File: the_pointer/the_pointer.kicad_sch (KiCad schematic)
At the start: 19 parts, among them U1 ESP32-S2FH4, U10 TPS61033DRLR, U101 ESP32-S3FN8, U2 W25Q128JVS, X2 XRCGB40M000F1S2GR0

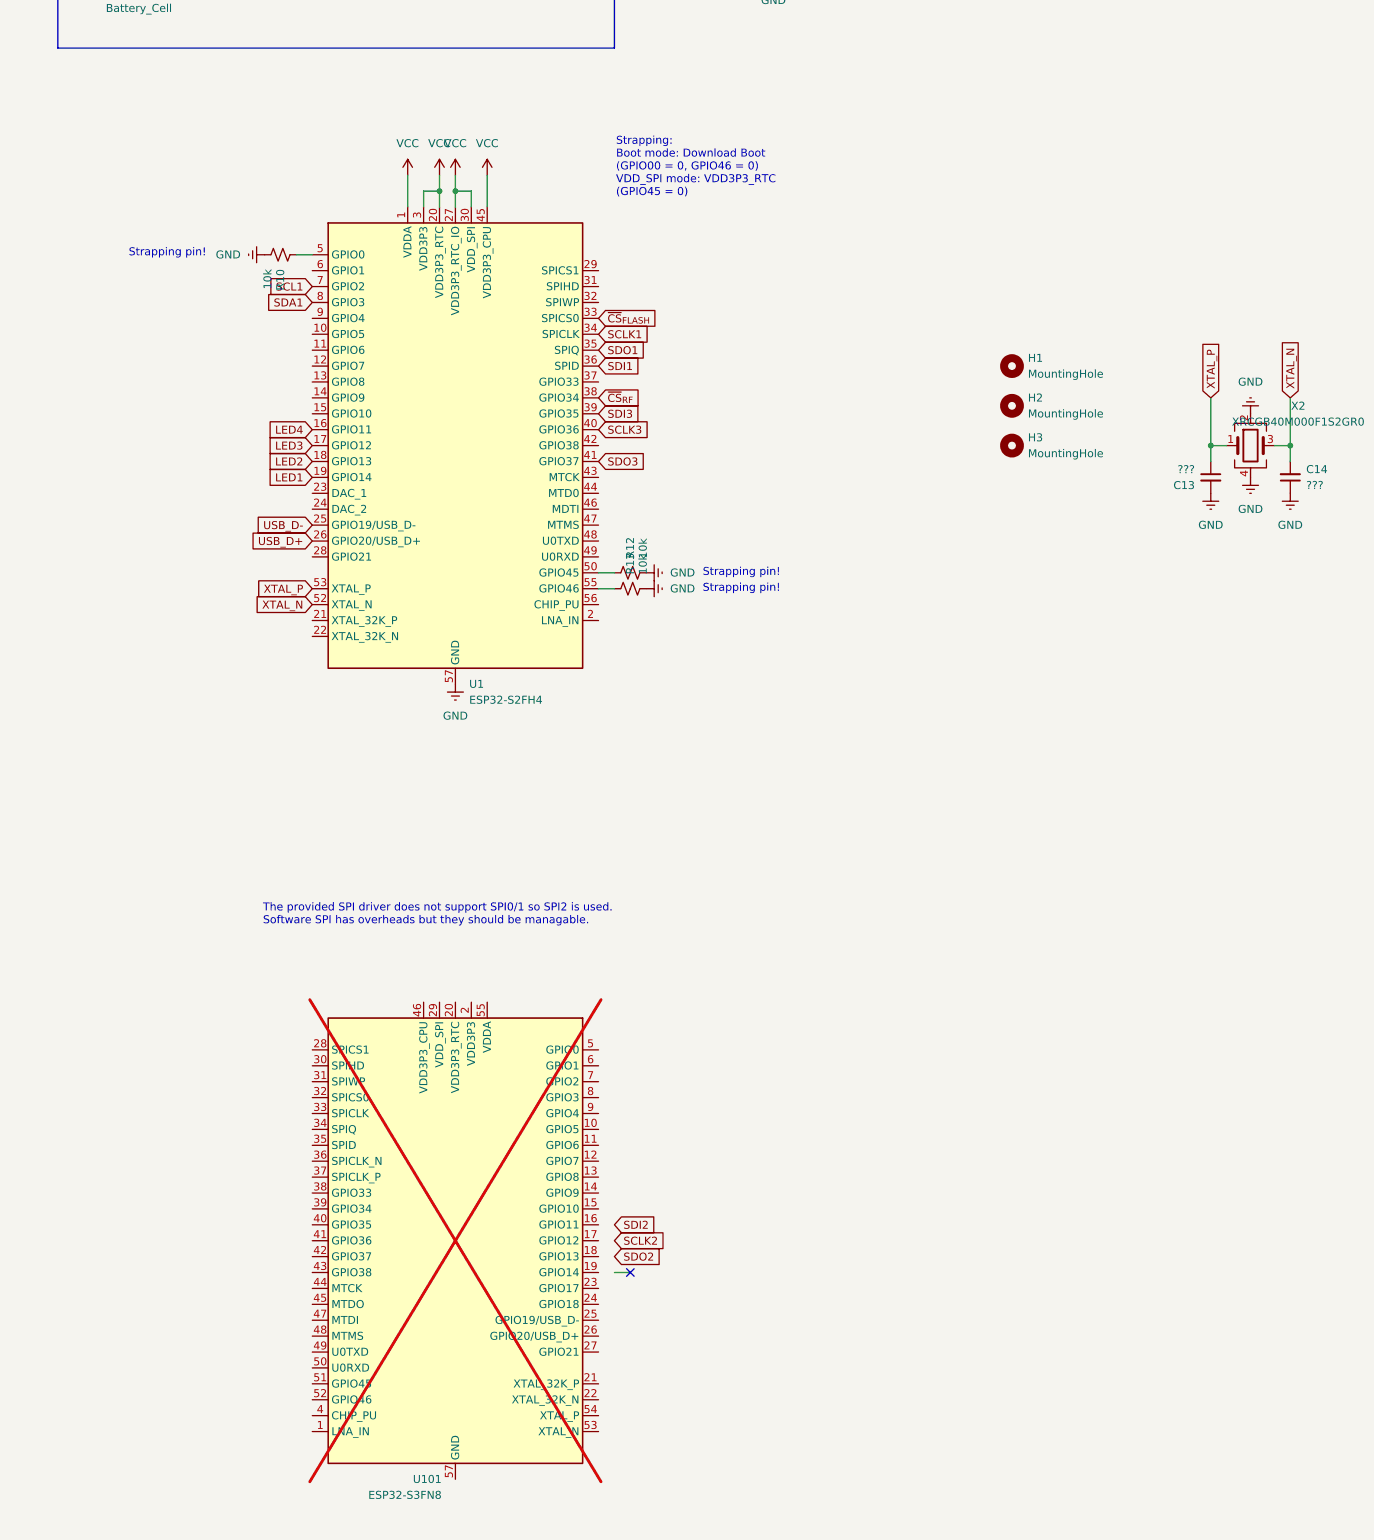
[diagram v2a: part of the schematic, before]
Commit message: Swapped Pointer to ESP32-C3FH4
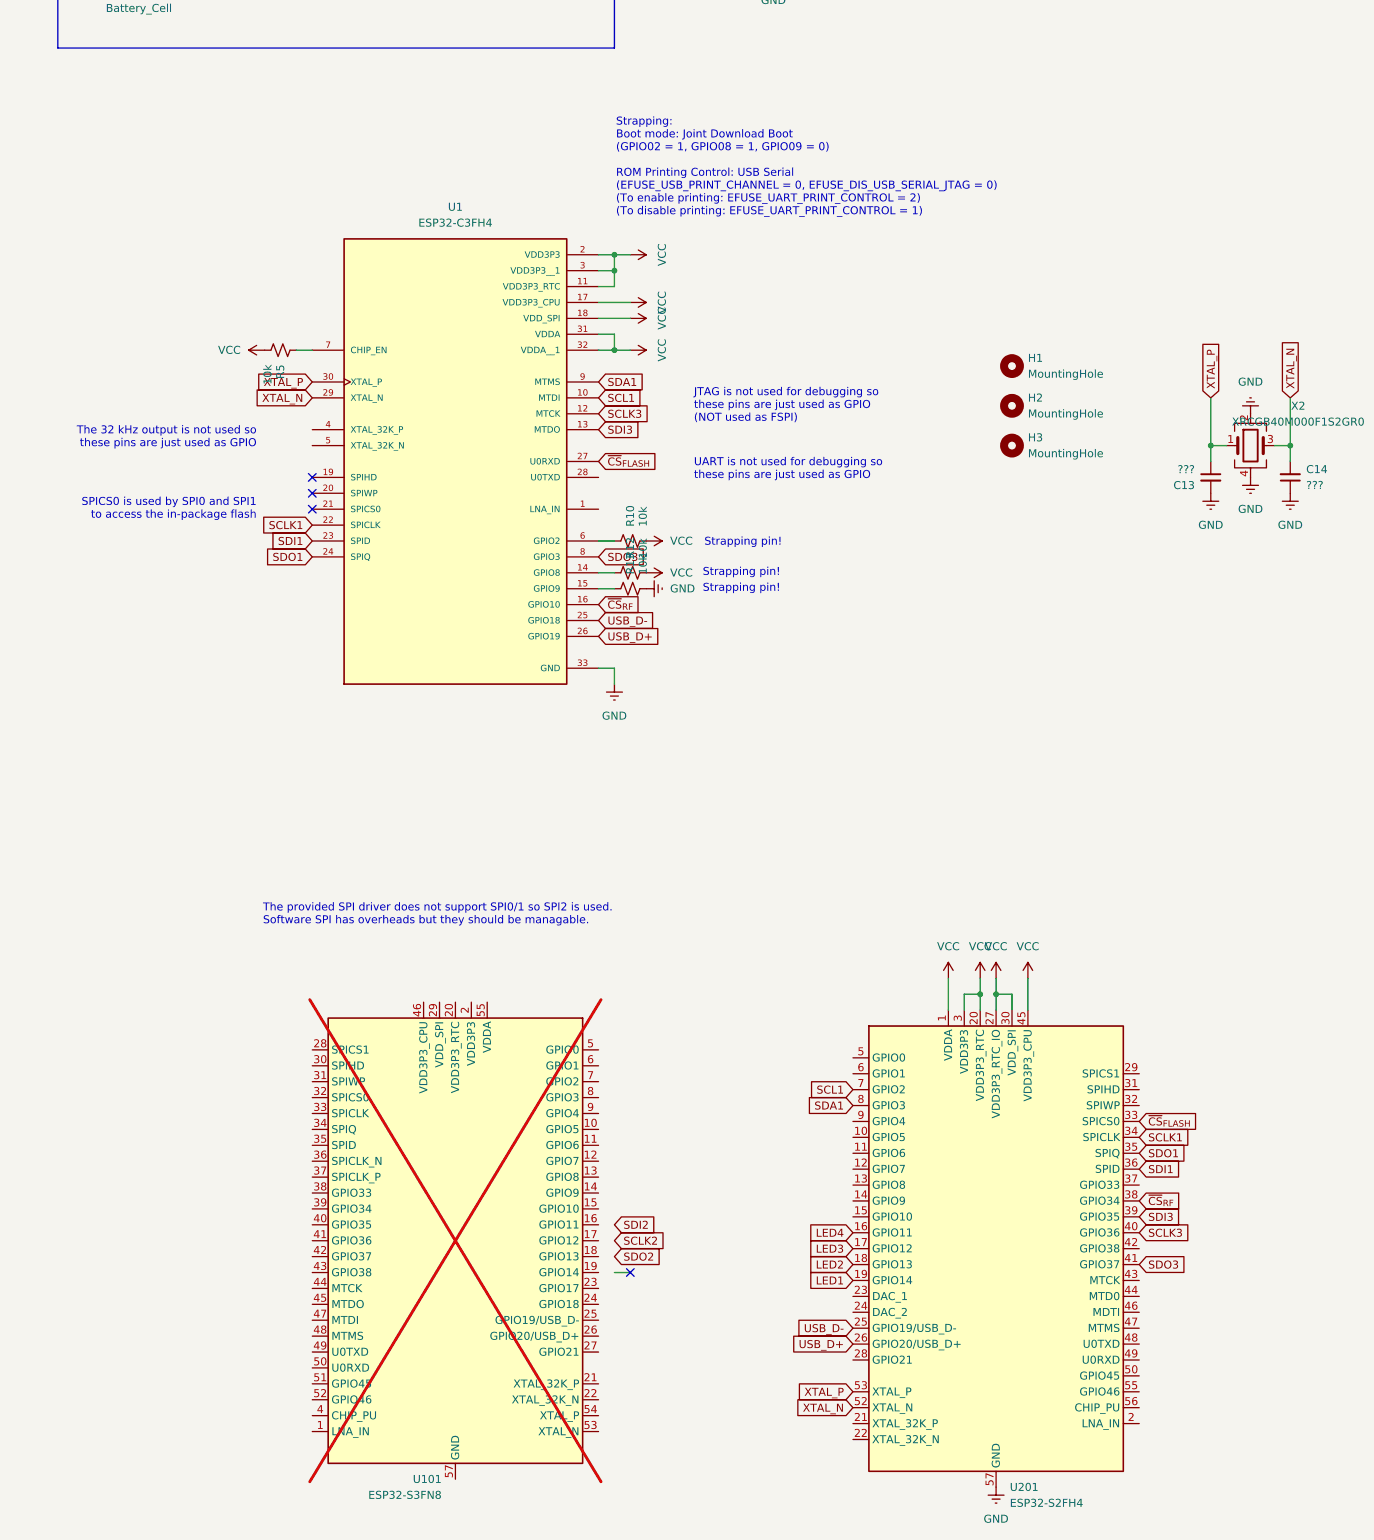
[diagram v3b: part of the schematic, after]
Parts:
- added R5: 10k, Resistor_SMD:R_0603_1608Metric, symbol Device:R_Small_US
- added U1: ESP32-C3FH4, Package_DFN_QFN:QFN-32-1EP_5x5mm_P0.5mm_EP3.7x3.7mm, symbol Custom_Flight_Computer_Symbols:ESP32-C3FH4
- renumbered U1 to U201
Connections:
- net GND: now also U1.33 (GND); no longer R10.2, R12.2
- net SCL1: now also U1.10 (MTDI)
- net SCLK1: now also U1.22 (SPICLK)
- net SCLK3: now also U1.12 (MTCK)
- net SDA1: now also U1.9 (MTMS)
- net SDI1: now also U1.23 (SPID)
- net SDI3: now also U1.13 (MTDO)
- net SDO1: now also U1.24 (SPIQ)
- net SDO3: now also U1.8 (GPIO3)
- net USB_D+: now also U1.26 (GPIO19)
- net USB_D-: now also U1.25 (GPIO18)
- net VCC: now also R10.2, R12.2, R5.2, U1.11 (VDD3P3_RTC), U1.17 (VDD3P3_CPU), U1.18 (VDD_SPI), U1.2 (VDD3P3), U1.3 (VDD3P3__1), U1.31 (VDDA), U1.32 (VDDA__1)
- net XTAL_N: now also U1.29 (XTAL_N)
- net XTAL_P: now also U1.30 (XTAL_P)
- net ~{CS}_{FLASH}: now also U1.27 (U0RXD)
- net ~{CS}_{RF}: now also U1.16 (GPIO10)
- net at R10.1: now also U1.6 (GPIO2); no longer U201.5 (GPIO0)
- net at R12.1: now also U1.14 (GPIO8); no longer U201.50 (GPIO45)
- net at U201.55 (GPIO46): no longer R13.1
- new net: R5.1, U1.7 (CHIP_EN)
- new net: R13.1, U1.15 (GPIO9)
- no-connect marks 1 -> 4
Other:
- note added: "JTAG is not used for debugging so these pins are just used as GPIO (NOT used as FSPI)"
- note added: "SPICS0 is used by SPI0 and SPI1 to access the in-package flash"
- note added: "Strapping: Boot mode: Joint Download Boot (GPIO02 = 1, GPIO08 = 1, GPIO09 = 0) ROM Printing Control: USB Serial (EFUSE_USB_PRINT_CHANNEL = 0, EFUSE_DIS_USB_SERIAL_JTAG = 0) (To enable printing: EFUSE_UART_PRINT_CONTROL = 2) (To disable printing: EFUSE_UART_PRINT_CONTROL = 1)"
- note added: "The 32 kHz output is not used so these pins are just used as GPIO"
- note added: "UART is not used for debugging so these pins are just used as GPIO"
- note removed: "Strapping: Boot mode: Download Boot (GPIO00 = 0, GPIO46 = 0) VDD_SPI mode: VDD3P3_RTC (GPIO45 = 0)"
- moved on the sheet: R10, U201
